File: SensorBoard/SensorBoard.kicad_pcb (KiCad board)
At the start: 2 copper layers, 50 x 50 mm, 9 parts, among them P1 CONN_01X07, P2 DHT22, P3 GY-87, P4 CONN_01X04, P5 CONN_01X07, P6 CONN_01X04

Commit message: Added labels pinout SensorBoard
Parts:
- moved REF** 6.05 mm to (93.2, 58.6)
- moved G*** 5.63 mm to (93.4, 94.0)
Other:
- board text added: "+BATT GND"
- board text added: "3.3V +BATT"
- board text added: "A3 A2 A1 A0"
- board text added: "D6/DHT"
- board text added: "D8 D7"
- board text added: "DRDY INTA"
- board text added: "FSYNC SDA"
- board text added: "GND +BATT"
- board text added: "INT1 INT0"
- board text added: "MOSI NSS"
- board text added: "RST"
- board text added: "SCK MISO"
- board text added: "SCL GND"
- board text added: "SCL SDA"
- board text added: "S_RX S_TX"
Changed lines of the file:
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@@
     (area 72.074999 50.674999 122.225001 100.825001)
     (thickness 1.6)
-    (drawings 23)
+    (drawings 38)
     (tracks 40)
     (zones 0)
@@
       (effects (font (size 1 1) (thickness 0.15)))
     )
-    (fp_text value GY-87 (at 2.65 9.86 270) (layer F.SilkS)
+    (fp_text value GY-87 (at -2.15 10.06 270) (layer F.SilkS)
       (effects (font (size 1 1) (thickness 0.15)))
     )
@@
   )
   (module theinventorhouse:electronic_cats_logo_8x6 (layer B.Cu)
-    (at 88 92.4 180)
+    (at 93.4 94 180)
     (fp_text reference G*** (at 0 0 180) (layer B.SilkS) hide
       (effects (font (thickness 0.3)) (justify mirror))
@@
   )
   (module Symbols:Symbol_OSHW-Logo_SilkScreen_BIG (layer B.Cu)
-    (at 92.4 52.6 180)
+    (at 93.2 58.6 180)
     (descr "Symbol, OSHW-Logo, Silk Screen, BIG")
     (tags "Symbol, OSHW-Logo, Silk Screen, BIG")
@@
     (fp_line (start -1.99898 -23.50008) (end -1.09982 -21.20138) (layer B.SilkS) (width 0.15))
   )
-  (gr_text "Sensor Board\nCaTSat 1.1v" (at 104.4 64.4) (layer B.SilkS)
+  (gr_text "INT1\nINT0" (at 87 57 90) (layer B.SilkS)
+    (effects (font (size 1.2 1.2) (thickness 0.3)) (justify mirror))
+  )
+  (gr_text "D8\nD7" (at 82 56.8 90) (layer B.SilkS)
+    (effects (font (size 1.2 1.2) (thickness 0.3)) (justify mirror))
+  )
+  (gr_text "3.3V\n+BATT" (at 112.4 75.4) (layer F.SilkS)
+    (effects (font (size 1.2 1.2) (thickness 0.3)))
+  )
+  (gr_text "SCL\nGND\n" (at 113.2 69.8) (layer F.SilkS)
+    (effects (font (size 1.2 1.2) (thickness 0.3)))
+  )
+  (gr_text "FSYNC\nSDA" (at 112.8 64.4) (layer F.SilkS)
+    (effects (font (size 1.2 1.2) (thickness 0.3)))
+  )
+  (gr_text D6/DHT (at 118 56.2) (layer B.SilkS)
+    (effects (font (size 1.2 1.2) (thickness 0.3)) (justify mirror))
+  )
+  (gr_text "S_RX\nS_TX" (at 111.6 57.6 90) (layer B.SilkS)
+    (effects (font (size 1.2 1.2) (thickness 0.3)) (justify mirror))
+  )
+  (gr_text "SCL\nSDA" (at 106.4 57 90) (layer B.SilkS)
+    (effects (font (size 1.2 1.2) (thickness 0.3)) (justify mirror))
+  )
+  (gr_text RST (at 78.8 94.8) (layer B.SilkS)
+    (effects (font (size 1.2 1.2) (thickness 0.3)) (justify mirror))
+  )
+  (gr_text "MOSI\nNSS" (at 79 90.6) (layer B.SilkS)
+    (effects (font (size 1.2 1.2) (thickness 0.3)) (justify mirror))
+  )
+  (gr_text "SCK\nMISO\n" (at 79 85.4) (layer B.SilkS)
+    (effects (font (size 1.2 1.2) (thickness 0.3)) (justify mirror))
+  )
+  (gr_text "+BATT\nGND" (at 79.2 80.6) (layer B.SilkS)
+    (effects (font (size 1.2 1.2) (thickness 0.3)) (justify mirror))
+  )
+  (gr_text "GND\n+BATT" (at 101.4 57.8 90) (layer B.SilkS)
+    (effects (font (size 1.2 1.2) (thickness 0.25)) (justify mirror))
+  )
+  (gr_text "DRDY\nINTA" (at 113 59.6) (layer F.SilkS)
+    (effects (font (size 1.2 1.2) (thickness 0.3)))
+  )
+  (gr_text "A3\nA2\nA1\nA0" (at 78.6 63.8) (layer B.SilkS)
+    (effects (font (size 1.5 1.5) (thickness 0.3)) (justify mirror))
+  )
+  (gr_text "Sensor Board\nCaTSat 1.1v" (at 99.2 66.4) (layer B.SilkS)
     (effects (font (size 1.5 1.5) (thickness 0.3)) (justify mirror))
   )
@@
     (connect_pads (clearance 0.8))
     (min_thickness 0.254)
-    (fill (arc_segments 16) (thermal_gap 0.508) (thermal_bridge_width 0.508))
+    (fill yes (arc_segments 16) (thermal_gap 0.508) (thermal_bridge_width 0.508))
     (polygon
       (pts
@@
     (connect_pads (clearance 0.8))
     (min_thickness 0.254)
-    (fill (arc_segments 16) (thermal_gap 0.508) (thermal_bridge_width 0.508))
+    (fill yes (arc_segments 16) (thermal_gap 0.508) (thermal_bridge_width 0.508))
     (polygon
       (pts

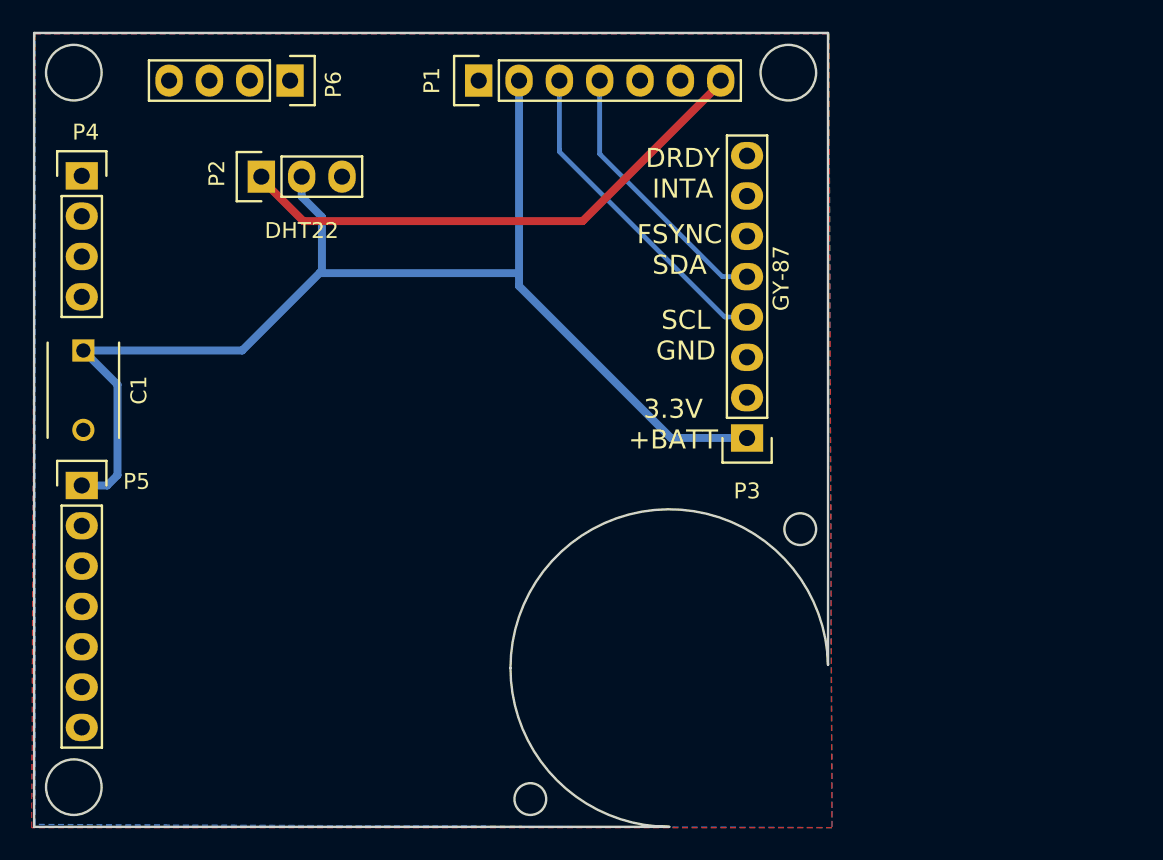
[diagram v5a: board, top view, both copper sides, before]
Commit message: Add larger holes
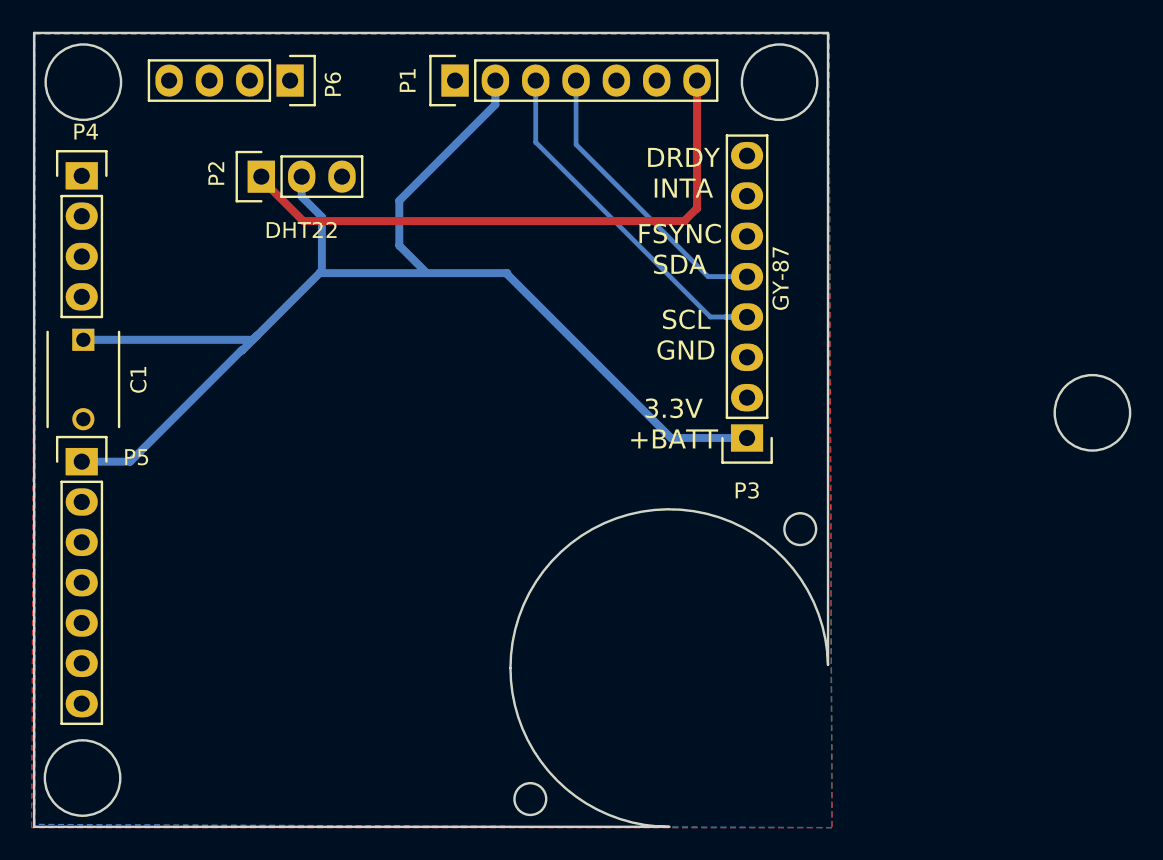
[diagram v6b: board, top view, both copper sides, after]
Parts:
- moved P5 1.50 mm to (75.2, 77.8)
- moved P1 1.49 mm to (98.7, 53.8)
- moved C1 0.67 mm to (75.2, 70.1)
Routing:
- net +BATT: track 116.4 -> 108.0 mm
- net /DHT/D6: track 34.1 -> 37.1 mm
- net /SCL: track 20.8 -> 22.3 mm
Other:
- board size 50 x 50 mm -> 69 x 50 mm
- board text added: "D6 DHT"
- board text removed: "D6/DHT"
